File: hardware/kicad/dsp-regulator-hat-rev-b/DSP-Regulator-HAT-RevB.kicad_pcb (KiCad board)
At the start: 2 copper layers, 100 x 102.6 mm, 163 parts, among them J1 FW-10-05-X-D-XXX-XXX-A, J10 1935161, J11 USB Hub I2C, J12 20021121-00010C4LF, J13 SWD_Debug_Header, J16 Conn_01x01_Pin, J17 Conn_01x01_Pin, J18 Conn_01x01_Pin, J19 SWD_Debug_Header, J2 FW-10-05-X-D-XXX-XXX-A, J20 Connector, USB-TYPE-C-16P, J21 Display Uart, J3 20021121-00010C4LF, J4 Fan Control, J5 Conn_01x01_Pin, J6 Conn_01x01_Pin, J7 Conn_01x01_Pin, J8 Conn_01x01_Pin, J9 1935161, Q1 PSMN5R2-60YL, Q10 PSMN5R2-60YL, Q2 PSMN5R2-60YL, Q3 PSMN5R2-60YL, Q4 PSMN5R2-60YL, Q5 AO3400A, Q7 PSMN5R2-60YL, Q8 PSMN5R2-60YL, Q9 PSMN5R2-60YL, U1 INA3221, U10 STM32_BLUE -, U11 W25Q128, U12 CH340C, U2 INA3221, U3 TLV1704AIPWR, U4 TLV1704AIPWR, U5 AHT20_C2757850, U7 74HC595D, U9 AMS1117-3.3

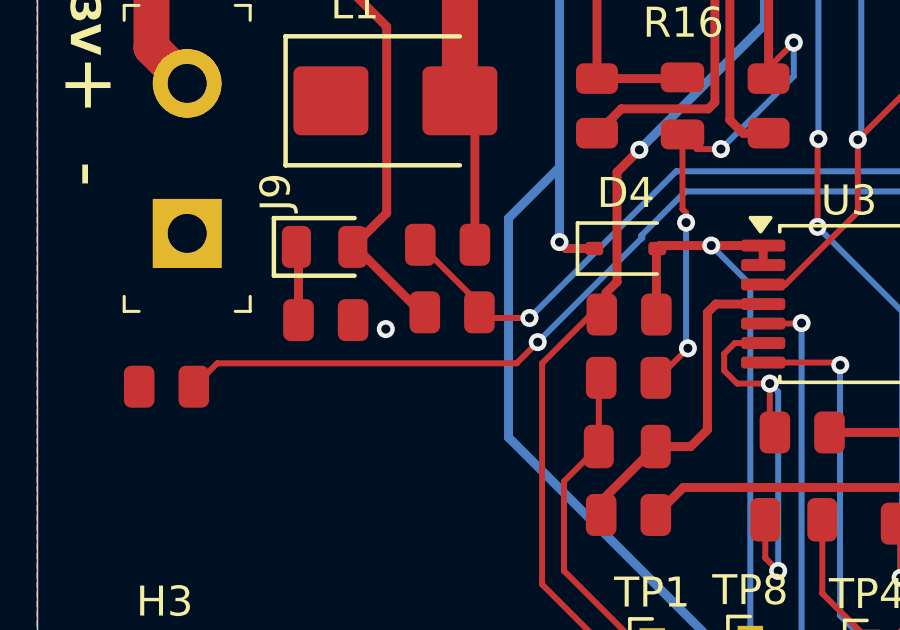
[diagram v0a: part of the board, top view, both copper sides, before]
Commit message: Add 2026-08-10 handoff and capture STM32/board debug state
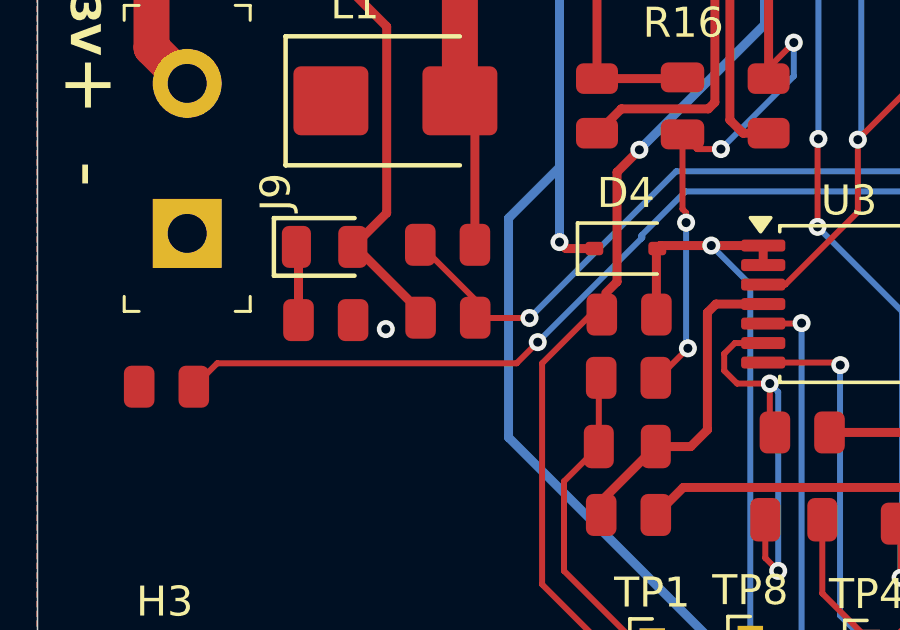
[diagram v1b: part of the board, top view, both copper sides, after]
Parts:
- moved R60 0.23 mm to (102.2, 125.5)
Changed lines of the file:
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@@
 	(footprint "PCM_JLCPCB:R_0805"
 		(layer "F.Cu")
-		(at 102.38 125.33)
+		(at 102.24 125.51)
 		(descr "Resistor SMD 0805 (2012 Metric), square (rectangular) end terminal, IPC_7351 nominal, (Body size source: IPC-SM-782 page 72, https://www.pcb-3d.com/wordpress/wp-content/uploads/ipc-sm-782a_amendment_1_and_2.pdf), generated with kicad-footprint-generator")
 		(tags "resistor")
@@
 	)
 	(segment
+		(start 104.96 125.52)
+		(end 103.48 125.52)
+		(width 0.2)
+		(layer "F.Cu")
+		(net 25)
+	)
+	(segment
 		(start 138.81 98.86)
 		(end 138.26 99.41)
@@
 	)
 	(segment
-		(start 103.29 125.05)
-		(end 101.32 123.08)
+		(start 103.48 125.52)
+		(end 103.47 125.51)
 		(width 0.2)
 		(layer "F.Cu")
@@
 	)
 	(segment
-		(start 138.76 96.89)
-		(end 138.81 96.94)
+		(start 103.15 125.51)
+		(end 103.29 125.37)
 		(width 0.2)
 		(layer "F.Cu")
@@
 	)
 	(segment
-		(start 103.48 125.52)
-		(end 103.29 125.33)
+		(start 103.29 125.37)
+		(end 103.29 125.05)
 		(width 0.2)
 		(layer "F.Cu")
@@
 	)
 	(segment
-		(start 103.29 125.33)
-		(end 103.29 125.05)
+		(start 103.47 125.51)
+		(end 103.15 125.51)
+		(width 0.2)
+		(layer "F.Cu")
+		(net 25)
+	)
+	(segment
+		(start 138.76 96.89)
+		(end 138.81 96.94)
 		(width 0.2)
 		(layer "F.Cu")
@@
 	)
 	(segment
-		(start 104.96 125.52)
-		(end 103.48 125.52)
+		(start 103.29 125.05)
+		(end 101.32 123.08)
 		(width 0.2)
 		(layer "F.Cu")
@@
 	)
 	(segment
-		(start 99.16 123.15)
-		(end 99.07 123.15)
+		(start 101.33 125.51)
+		(end 101.34 125.5)
 		(width 0.3)
 		(layer "F.Cu")
@@
 	)
 	(segment
-		(start 101.47 125.33)
-		(end 101.34 125.33)
+		(start 101.34 125.33)
+		(end 99.16 123.15)
 		(width 0.3)
 		(layer "F.Cu")
@@
 	)
 	(segment
-		(start 101.34 125.33)
-		(end 99.16 123.15)
+		(start 101.34 125.5)
+		(end 101.34 125.33)
+		(width 0.3)
+		(layer "F.Cu")
+		(net 39)
+	)
+	(segment
+		(start 99.16 123.15)
+		(end 99.07 123.15)
 		(width 0.3)
 		(layer "F.Cu")
@@
 		(min_thickness 0.25)
 		(filled_areas_thickness no)
-		(fill yes
+		(fill
 			(thermal_gap 0.5)
 			(thermal_bridge_width 0.5)
